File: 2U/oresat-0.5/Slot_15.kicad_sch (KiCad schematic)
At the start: 2 parts

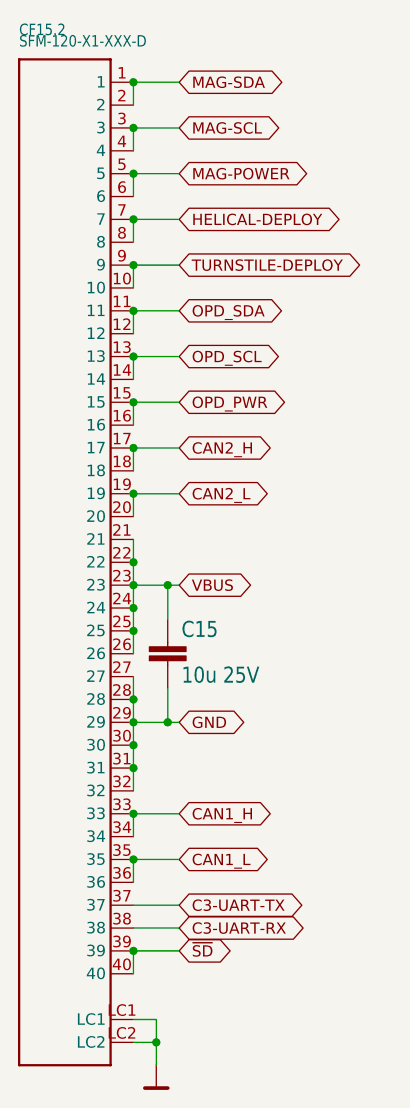
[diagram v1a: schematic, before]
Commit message: Fixed all (most) of the issues from Eagle imports
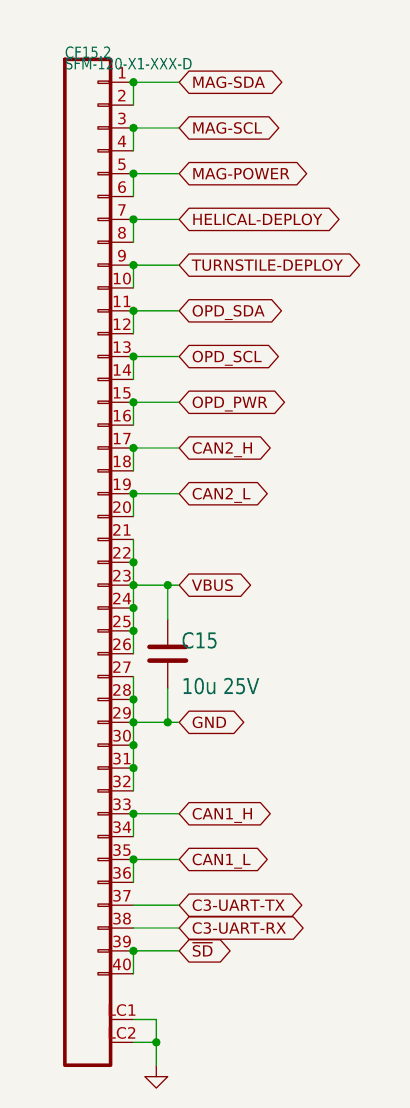
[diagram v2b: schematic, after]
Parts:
- C15: symbol oresat0-1u-backplane-eagle-import:C-EU1206-B -> Device:C
- CF15.2: symbol oresat-backplane-2u-eagle-import:SFM-120-X1-XXX-D -> oresat-connectors:J-SAMTEC-TFM-120-01-L-D-RA

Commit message: Moved entire schematic to single page
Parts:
- removed C15: 10u 25V, Capacitor_SMD:C_1206_3216Metric, symbol Device:C
- removed CF15.2: SFM-120-X1-XXX-D, oresat-connectors:J-SAMTEC-SFM-120-X1-XXX-D, symbol oresat-connectors:J-SAMTEC-TFM-120-01-L-D-RA
